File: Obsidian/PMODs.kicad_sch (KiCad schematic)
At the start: 6 parts, among them J14 Conn_02x06_Top_Bottom, J15 Conn_02x06_Top_Bottom, J4 Conn_02x06_Top_Bottom, J5 Conn_02x06_Top_Bottom, J6 Conn_02x06_Top_Bottom, J7 Conn_02x06_Top_Bottom

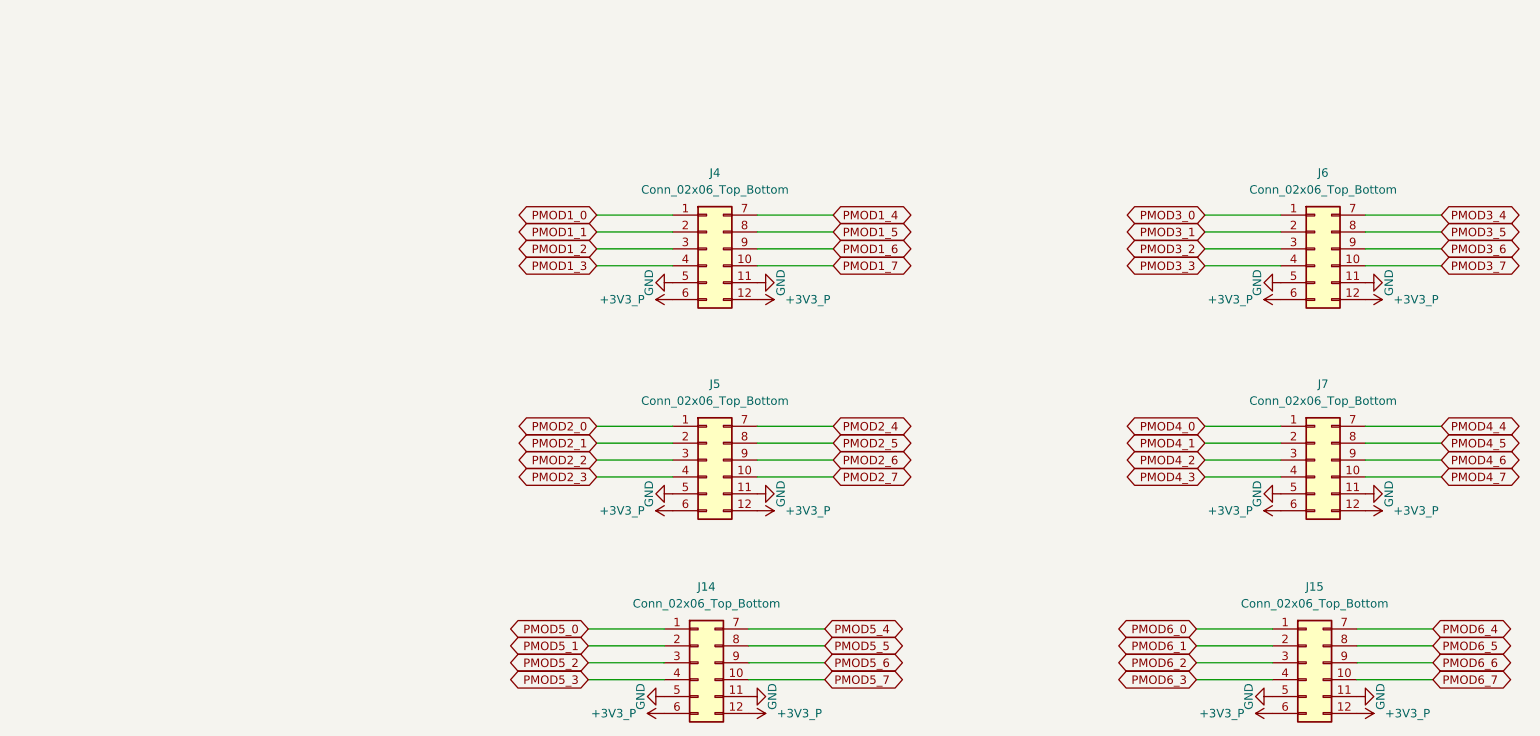
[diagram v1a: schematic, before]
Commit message: replacing global label with hierarchical label
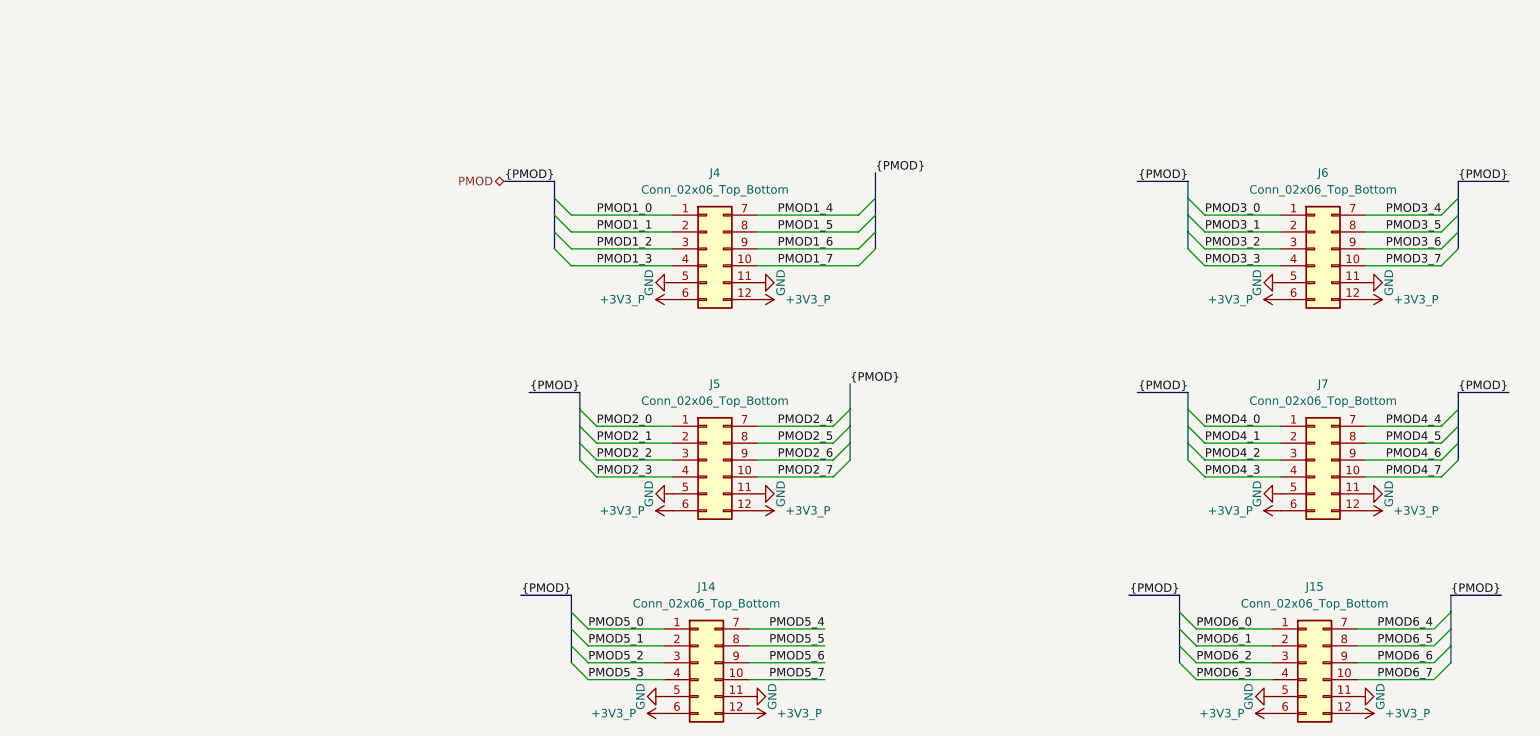
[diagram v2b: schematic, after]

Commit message: Adding symbol library
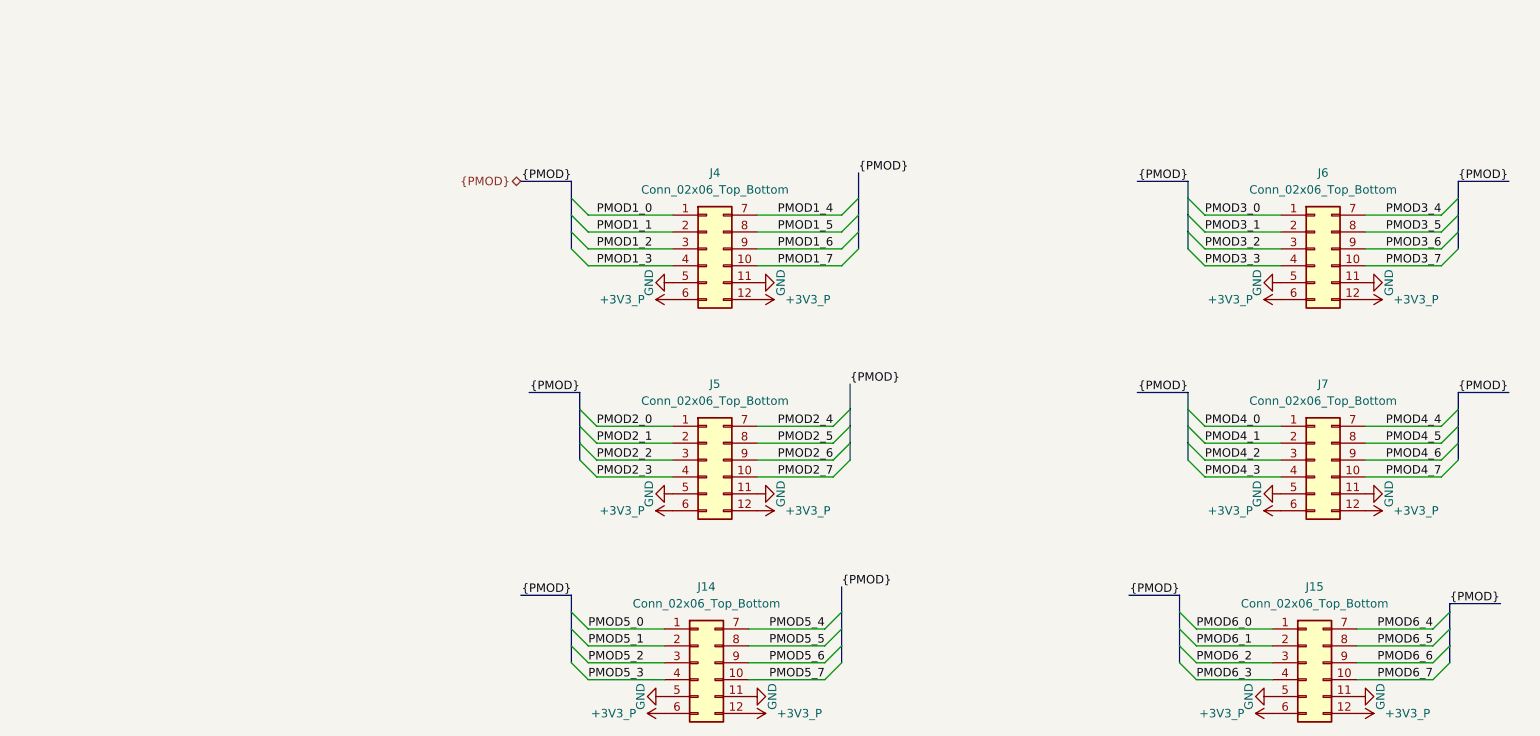
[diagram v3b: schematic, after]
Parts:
- J14, J15, J4, J5, J6, J7: symbol Connector_Generic:Conn_02x06_Top_Bottom -> Library_Symbol:Conn_02x06_Top_Bottom

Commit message: Correct Schematic errors
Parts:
- J14, J15: footprint Miscellaneous THD:PinSocket_2x06_P2.54mm_Vertical_PMOD -> Footprint:PinSocket_2x06_P2.54mm_Horizontal_PMOD
- J4, J5, J6, J7: footprint Miscellaneous THD:PinSocket_2x06_P2.54mm_Horizontal_PMOD -> Footprint:PinSocket_2x06_P2.54mm_Horizontal_PMOD
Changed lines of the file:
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@@
 			)
 		)
-		(property "Footprint" "Miscellaneous THD:PinSocket_2x06_P2.54mm_Horizontal_PMOD"
+		(property "Footprint" "Footprint:PinSocket_2x06_P2.54mm_Horizontal_PMOD"
 			(at 119.38 55.88 0)
 			(effects
@@
 			)
 		)
-		(property "Footprint" "Miscellaneous THD:PinSocket_2x06_P2.54mm_Horizontal_PMOD"
+		(property "Footprint" "Footprint:PinSocket_2x06_P2.54mm_Horizontal_PMOD"
 			(at 210.82 55.88 0)
 			(effects
@@
 			)
 		)
-		(property "Footprint" "Miscellaneous THD:PinSocket_2x06_P2.54mm_Horizontal_PMOD"
+		(property "Footprint" "Footprint:PinSocket_2x06_P2.54mm_Horizontal_PMOD"
 			(at 210.82 87.63 0)
 			(effects
@@
 			)
 		)
-		(property "Footprint" "Miscellaneous THD:PinSocket_2x06_P2.54mm_Vertical_PMOD"
+		(property "Footprint" "Footprint:PinSocket_2x06_P2.54mm_Horizontal_PMOD"
 			(at 118.11 118.11 0)
 			(effects
@@
 			)
 		)
-		(property "Footprint" "Miscellaneous THD:PinSocket_2x06_P2.54mm_Vertical_PMOD"
+		(property "Footprint" "Footprint:PinSocket_2x06_P2.54mm_Horizontal_PMOD"
 			(at 209.55 118.11 0)
 			(effects
@@
 			)
 		)
-		(property "Footprint" "Miscellaneous THD:PinSocket_2x06_P2.54mm_Horizontal_PMOD"
+		(property "Footprint" "Footprint:PinSocket_2x06_P2.54mm_Horizontal_PMOD"
 			(at 119.38 87.63 0)
 			(effects

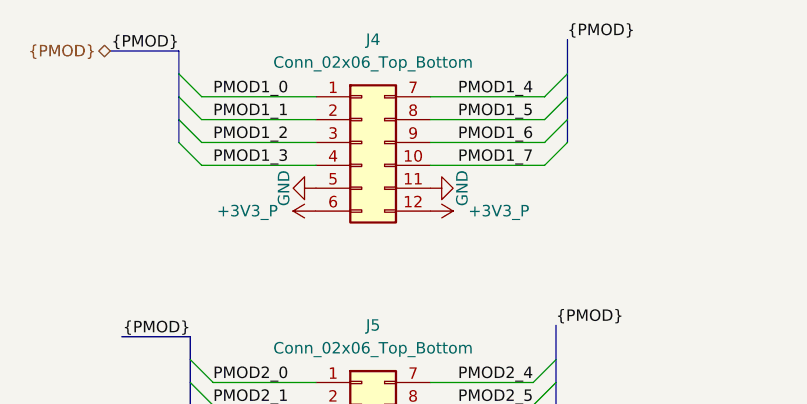
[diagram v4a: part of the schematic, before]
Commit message: Changed layout in a way TWIST and Obsidian are aligned properly.
Signed-off-by: Jean Alinei <jean.alinei@owntech.org>
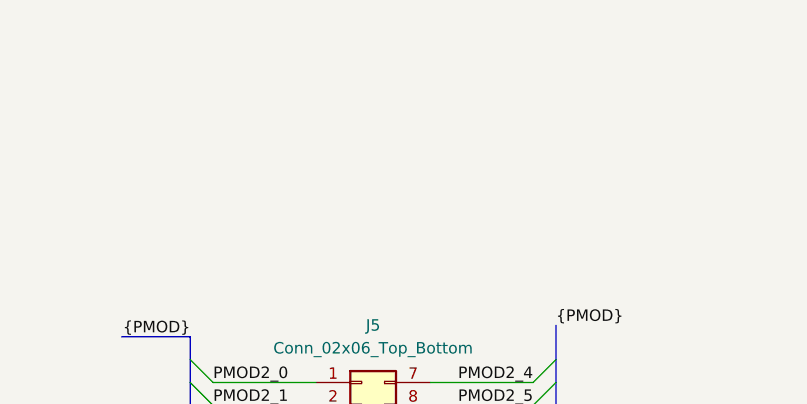
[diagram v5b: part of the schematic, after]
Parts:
- removed J4: Conn_02x06_Top_Bottom, Footprint:PinSocket_2x06_P2.54mm_Horizontal_PMOD, symbol Library_Symbol:Conn_02x06_Top_Bottom

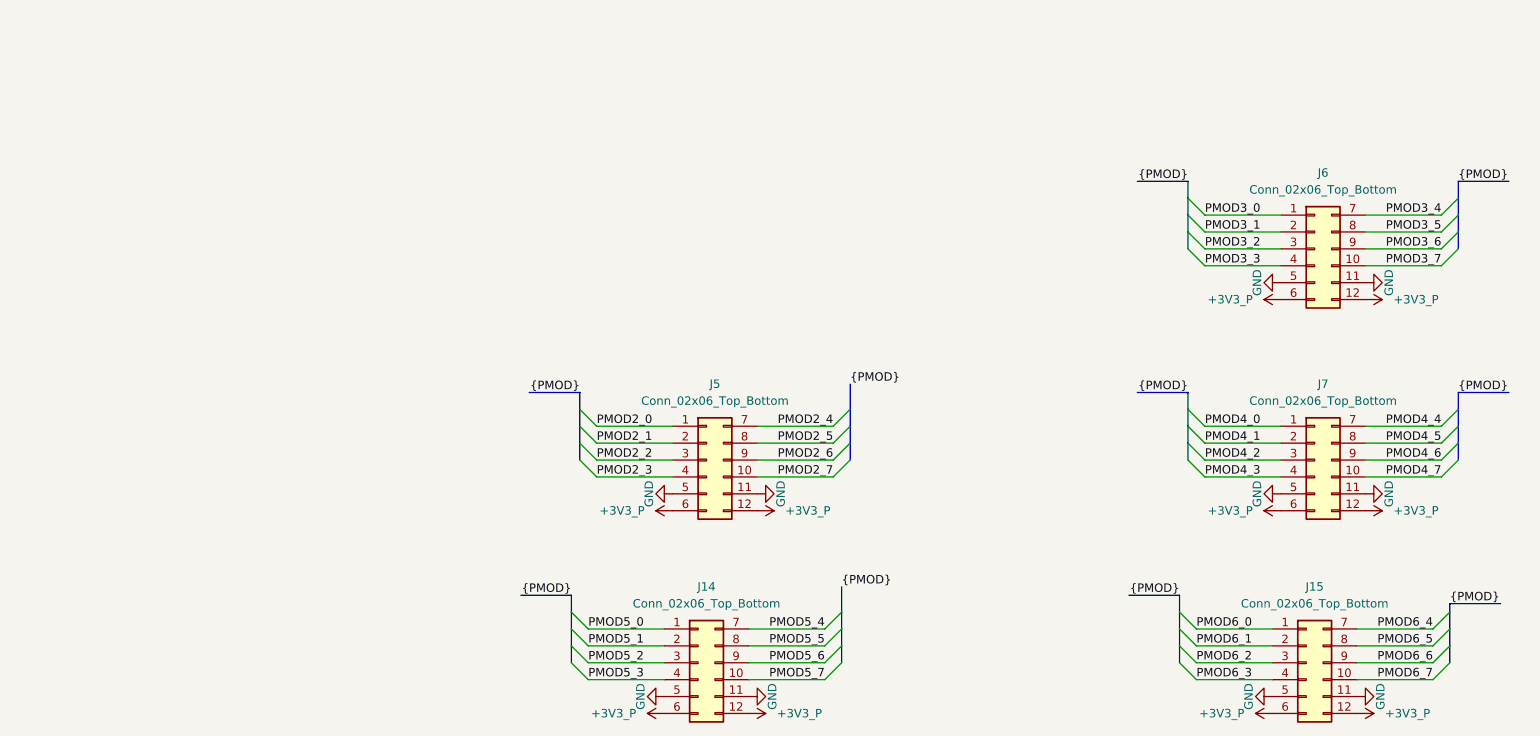
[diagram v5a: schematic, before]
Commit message: adding flex connector
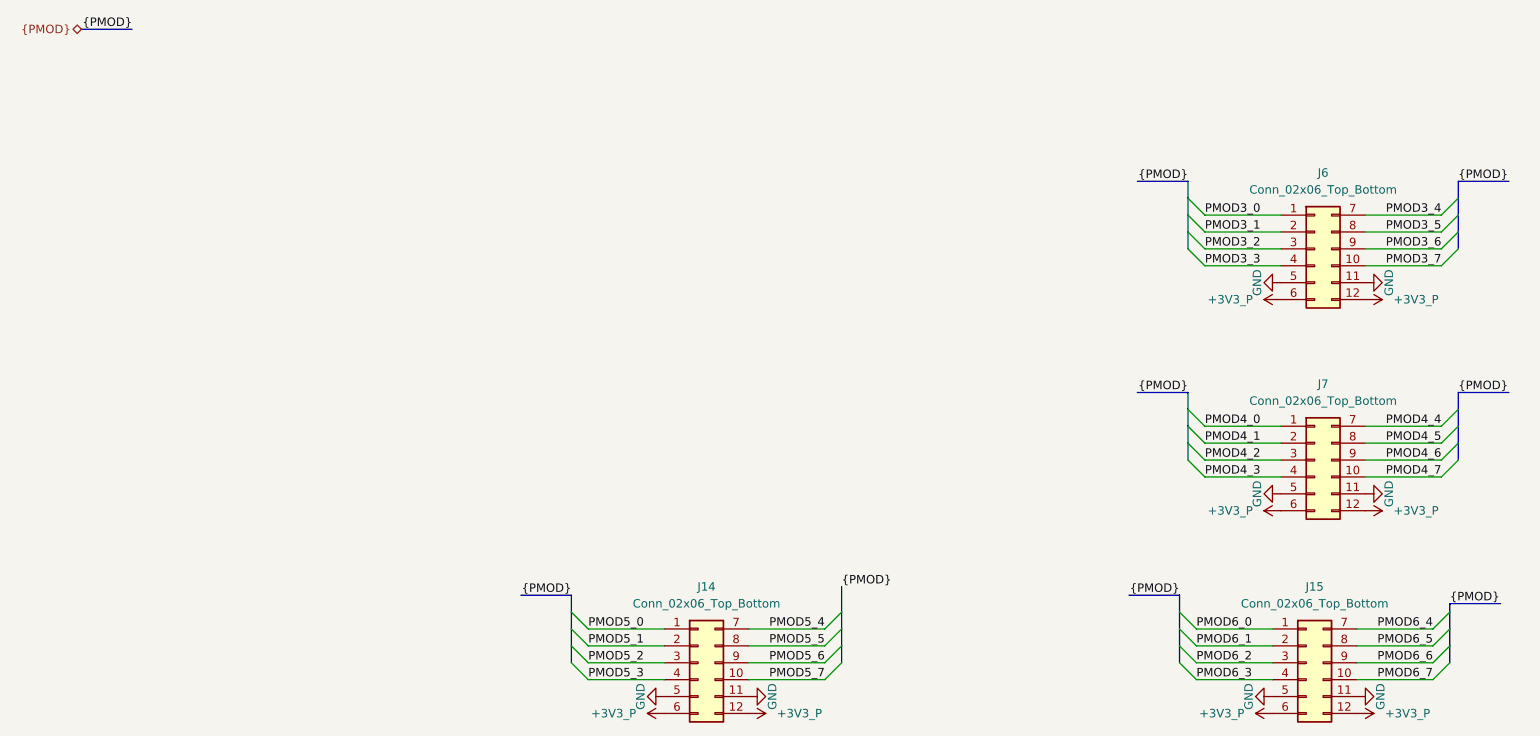
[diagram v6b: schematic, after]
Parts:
- removed J5: Conn_02x06_Top_Bottom, Footprint:PinSocket_2x06_P2.54mm_Horizontal_PMOD, symbol Library_Symbol:Conn_02x06_Top_Bottom

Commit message: adding lcsc reference for PMOD
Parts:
- J14, J15, J6, J7: LCSC (none) -> C5333437

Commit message: update LCSC reference, and OFFSET rotation for JLCPCB
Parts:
- J14, J15, J6, J7: FT Rotation Offset (none) -> 270
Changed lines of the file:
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@@
 			)
 		)
-		(property "FT Rotation Offset" ""
+		(property "FT Rotation Offset" "270"
 			(at 210.82 55.88 0)
 			(effects
@@
 			)
 		)
-		(property "FT Rotation Offset" ""
+		(property "FT Rotation Offset" "270"
 			(at 210.82 87.63 0)
 			(effects
@@
 			)
 		)
-		(property "FT Rotation Offset" ""
+		(property "FT Rotation Offset" "270"
 			(at 118.11 118.11 0)
 			(effects
@@
 			)
 		)
-		(property "FT Rotation Offset" ""
+		(property "FT Rotation Offset" "270"
 			(at 209.55 118.11 0)
 			(effects
